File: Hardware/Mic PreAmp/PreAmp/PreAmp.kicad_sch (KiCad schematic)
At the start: 1 part, among them U1 INA217AIDWR

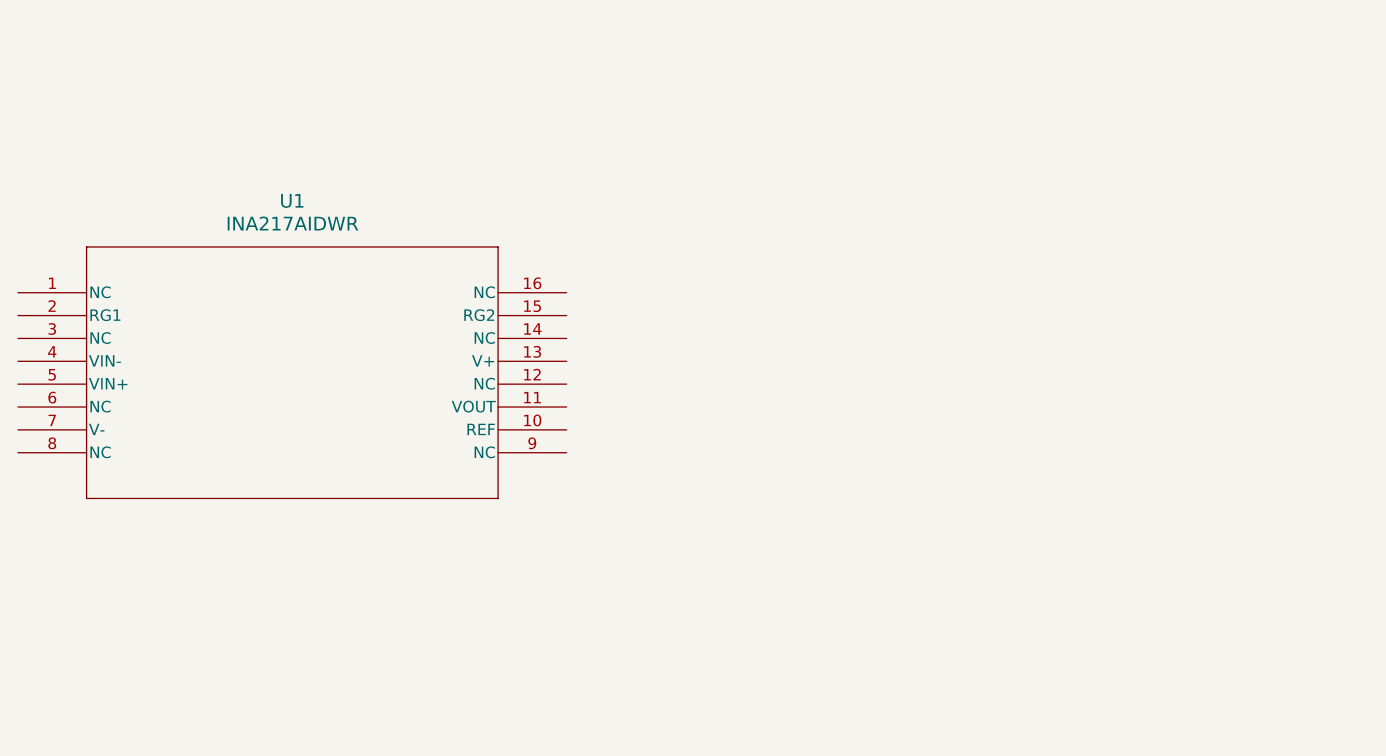
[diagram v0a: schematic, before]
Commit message: Header pins for input and output
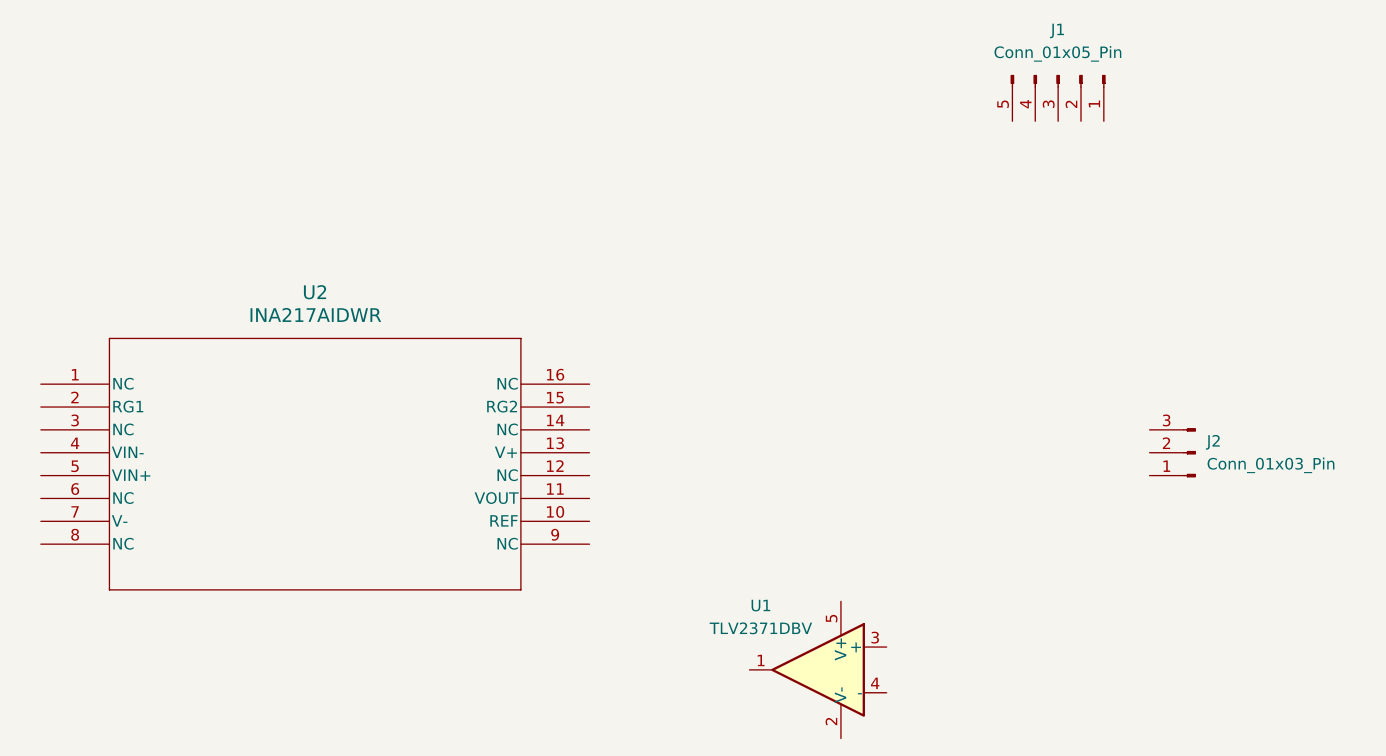
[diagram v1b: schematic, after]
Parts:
- removed U1: INA217AIDWR, DW16, symbol INA217:INA217AIDWR
- added J1: Conn_01x05_Pin, Connector_PinSocket_2.54mm:PinSocket_1x05_P2.54mm_Vertical, symbol Connector:Conn_01x05_Pin
- added J2: Conn_01x03_Pin, symbol Connector:Conn_01x03_Pin
- added U1: TLV2371DBV, Package_TO_SOT_SMD:SOT-23-5, symbol Amplifier_Operational:TLV2371DBV
- added U2: INA217AIDWR, INA217:DW16, symbol INA217:INA217AIDWR
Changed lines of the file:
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@@
 	)
 	(symbol
-		(lib_id "INA217:INA217AIDWR")
-		(at 106.68 81.28 0)
+		(lib_id "Connector:Conn_01x03_Pin")
+		(at 237.49 99.06 180)
 		(unit 1)
 		(exclude_from_sim no)
@@
 		(dnp no)
 		(fields_autoplaced yes)
+		(property "Reference" "J2"
+			(at 238.76 97.7899 0)
+			(effects
+				(font
+					(size 1.27 1.27)
+				)
+				(justify right)
+			)
+		)
+		(property "Value" "Conn_01x03_Pin"
+			(at 238.76 100.3299 0)
+			(effects
+				(font
+					(size 1.27 1.27)
+				)
+				(justify right)
+			)
+		)
+		(property "Footprint" ""
+			(at 237.49 99.06 0)
+			(effects
+				(font
+					(size 1.27 1.27)
+				)
+				(hide yes)
+			)
+		)
+		(property "Datasheet" "~"
+			(at 237.49 99.06 0)
+			(effects
+				(font
+					(size 1.27 1.27)
+				)
+				(hide yes)
+			)
+		)
+		(property "Description" "Generic connector, single row, 01x03, script generated"
+			(at 237.49 99.06 0)
+			(effects
+				(font
+					(size 1.27 1.27)
+				)
+				(hide yes)
+			)
+		)
+		(pin "3"
+		)
+		(pin "2"
+		)
+		(pin "1"
+		)
+		(instances
+			(project ""
+				(path "/c83f892f-6017-40cb-88c0-c4e7a35464f0"
+					(reference "J2")
+					(unit 1)
+				)
+			)
+		)
+	)
+	(symbol
+		(lib_id "INA217:INA217AIDWR")
+		(at 109.22 91.44 0)
+		(unit 1)
+		(exclude_from_sim no)
+		(in_bom yes)
+		(on_board yes)
+		(dnp no)
+		(fields_autoplaced yes)
+		(property "Reference" "U2"
+			(at 139.7 81.28 0)
+			(effects
+				(font
+					(size 1.524 1.524)
+				)
+			)
+		)
+		(property "Value" "INA217AIDWR"
+			(at 139.7 83.82 0)
+			(effects
+				(font
+					(size 1.524 1.524)
+				)
+			)
+		)
+		(property "Footprint" "INA217:DW16"
+			(at 109.22 91.44 0)
+			(effects
+				(font
+					(size 1.27 1.27)
+					(italic yes)
+				)
+				(hide yes)
+			)
+		)
+		(property "Datasheet" "INA217AIDWR"
+			(at 109.22 91.44 0)
+			(effects
+				(font
+					(size 1.27 1.27)
+					(italic yes)
+				)
+				(hide yes)
+			)
+		)
+		(property "Description" ""
+			(at 109.22 91.44 0)
+			(effects
+				(font
+					(size 1.27 1.27)
+				)
+				(hide yes)
+			)
+		)
+		(pin "13"
+		)
+		(pin "11"
+		)
+		(pin "12"
+		)
+		(pin "3"
+		)
+		(pin "4"
+		)
+		(pin "5"
+		)
+		(pin "6"
+		)
+		(pin "7"
+		)
+		(pin "8"
+		)
+		(pin "1"
+		)
+		(pin "9"
+		)
+		(pin "14"
+		)
+		(pin "15"
+		)
+		(pin "2"
+		)
+		(pin "10"
+		)
+		(pin "16"
+		)
+		(instances
+			(project ""
+				(path "/c83f892f-6017-40cb-88c0-c4e7a35464f0"
+					(reference "U2")
+					(unit 1)
+				)
+			)
+		)
+	)
+	(symbol
+		(lib_id "Amplifier_Operational:TLV2371DBV")
+		(at 195.58 123.19 0)
+		(mirror y)
+		(unit 1)
+		(exclude_from_sim no)
+		(in_bom yes)
+		(on_board yes)
+		(dnp no)
 		(property "Reference" "U1"
-			(at 137.16 71.12 0)
-			(effects
-				(font
-					(size 1.524 1.524)
-				)
-			)
-		)
-		(property "Value" "INA217AIDWR"
-			(at 137.16 73.66 0)
-			(effects
-				(font
-					(size 1.524 1.524)
-				)
-			)
-		)
-		(property "Footprint" "DW16"
-			(at 106.68 81.28 0)
-			(effects
-				(font
-					(size 1.27 1.27)
-					(italic yes)
-				)
-				(hide yes)
-			)
-		)
-		(property "Datasheet" "INA217AIDWR"
-			(at 106.68 81.28 0)
-			(effects
-				(font
-					(size 1.27 1.27)
-					(italic yes)
-				)
-				(hide yes)
-			)
-		)
-		(property "Description" ""
-			(at 106.68 81.28 0)
+			(at 189.23 116.078 0)
+			(effects
+				(font
+					(size 1.27 1.27)
+				)
+			)
+		)
+		(property "Value" "TLV2371DBV"
+			(at 189.23 118.618 0)
+			(effects
+				(font
+					(size 1.27 1.27)
+				)
+			)
+		)
+		(property "Footprint" "Package_TO_SOT_SMD:SOT-23-5"
+			(at 198.12 128.27 0)
+			(effects
+				(font
+					(size 1.27 1.27)
+				)
+				(justify left)
+				(hide yes)
+			)
+		)
+		(property "Datasheet" "http://www.ti.com/lit/ds/symlink/tlv2375.pdf"
+			(at 195.58 118.11 0)
+			(effects
+				(font
+					(size 1.27 1.27)
+				)
+				(hide yes)
+			)
+		)
+		(property "Description" "Rail-to-Rail Input/Output Operational Amplifier, SOT-23-5"
+			(at 195.58 123.19 0)
 			(effects
 				(font
@@
 		(pin "3"
 		)
-		(pin "10"
-		)
-		(pin "15"
-		)
-		(pin "12"
-		)
-		(pin "11"
-		)
-		(pin "6"
-		)
-		(pin "7"
-		)
-		(pin "8"
-		)
-		(pin "16"
-		)
-		(pin "9"
+		(pin "5"
+		)
+		(pin "1"
+		)
+		(pin "4"
 		)
 		(pin "2"
-		)
-		(pin "4"
-		)
-		(pin "13"
-		)
-		(pin "5"
-		)
-		(pin "1"
-		)
-		(pin "14"
 		)
 		(instances
@@
 					(unit 1)
 				)
+			)
+		)
+	)
+	(symbol
+		(lib_id "Connector:Conn_01x05_Pin")
+		(at 222.25 57.15 270)
+		(unit 1)
+		(exclude_from_sim no)
+		(in_bom yes)
+		(on_board yes)
+		(dnp no)
+		(fields_autoplaced yes)
+		(property "Reference" "J1"
+			(at 222.25 52.07 90)
+			(effects
+				(font
+					(size 1.27 1.27)
+				)
+			)
+		)
+		(property "Value" "Conn_01x05_Pin"
+			(at 222.25 54.61 90)
+			(effects
+				(font
+					(size 1.27 1.27)
+				)
+			)
+		)
+		(property "Footprint" "Connector_PinSocket_2.54mm:PinSocket_1x05_P2.54mm_Vertical"
+			(at 222.25 57.15 0)
+			(effects
+				(font
+					(size 1.27 1.27)
+				)
+				(hide yes)
+			)
+		)
+		(property "Datasheet" "~"
+			(at 222.25 57.15 0)
+			(effects
+				(font
+					(size 1.27 1.27)
+				)
+				(hide yes)
+			)
+		)
+		(property "Description" "Generic connector, single row, 01x05, script generated"
+			(at 222.25 57.15 0)
+			(effects
+				(font
+					(size 1.27 1.27)
+				)
+				(hide yes)
+			)
+		)
+		(pin "2"
+		)
+		(pin "1"
+		)
+		(pin "5"
+		)
+		(pin "4"
+		)
+		(pin "3"
+		)
+		(instances
+			(project ""
+				(path "/c83f892f-6017-40cb-88c0-c4e7a35464f0"
+					(reference "J1")
+					(unit 1)
+				)

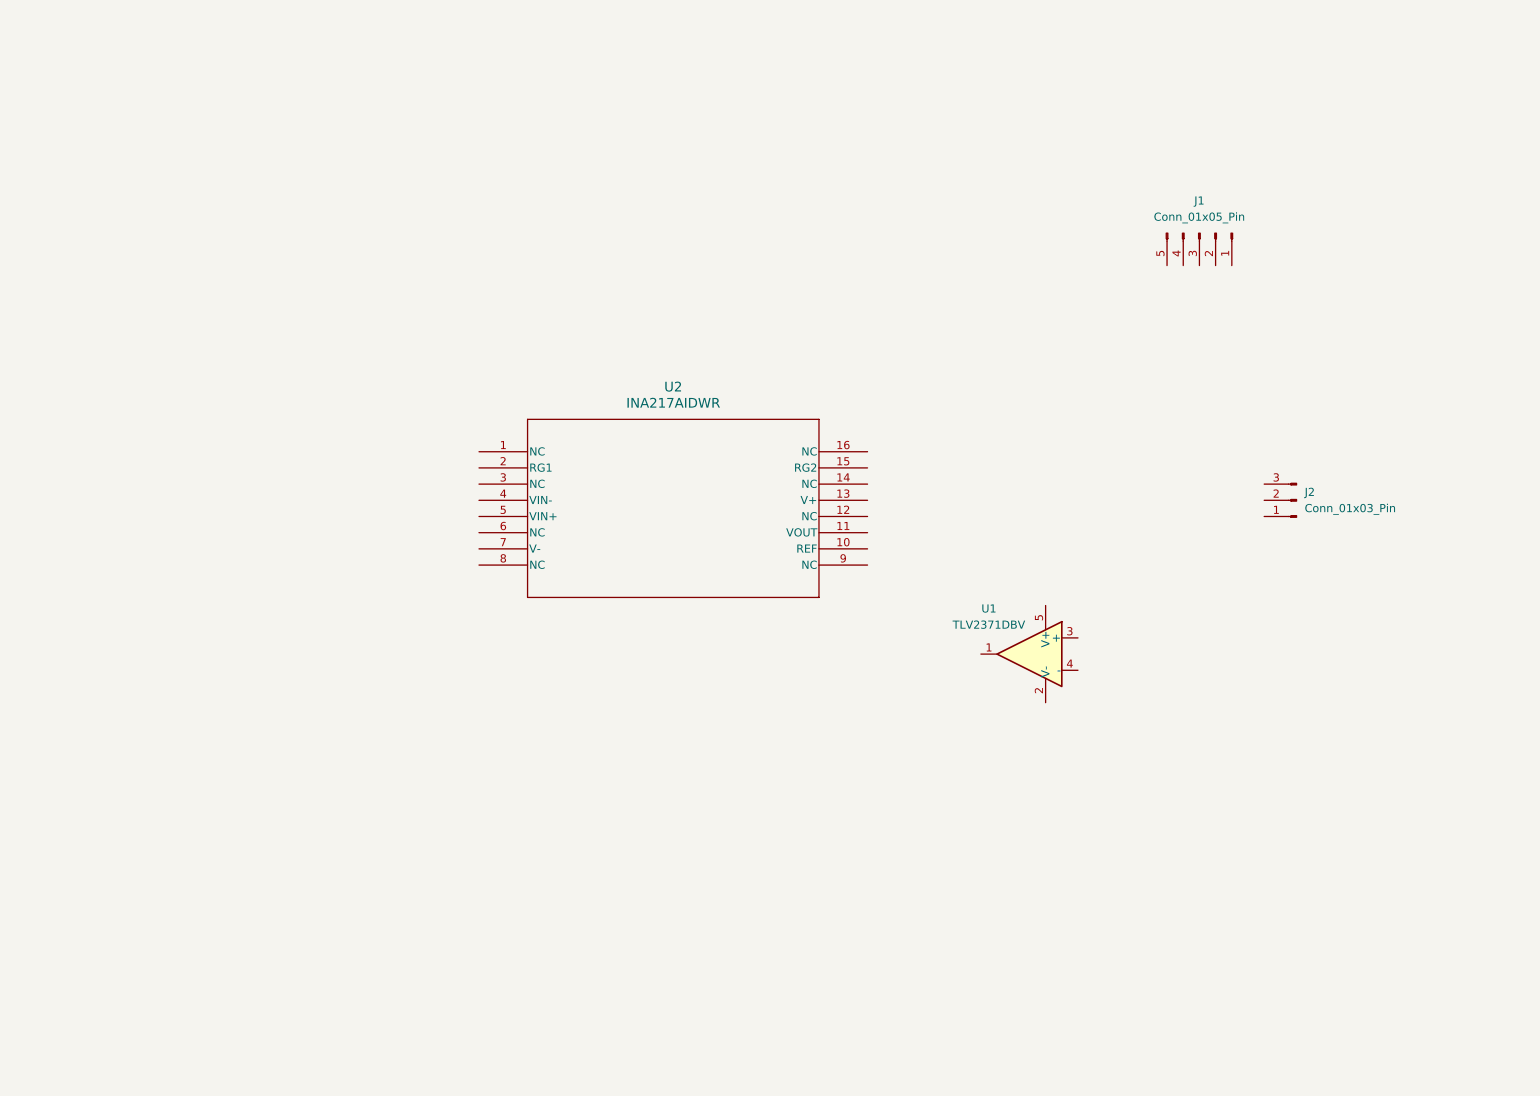
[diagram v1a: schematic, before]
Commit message: Inserted XLR plug
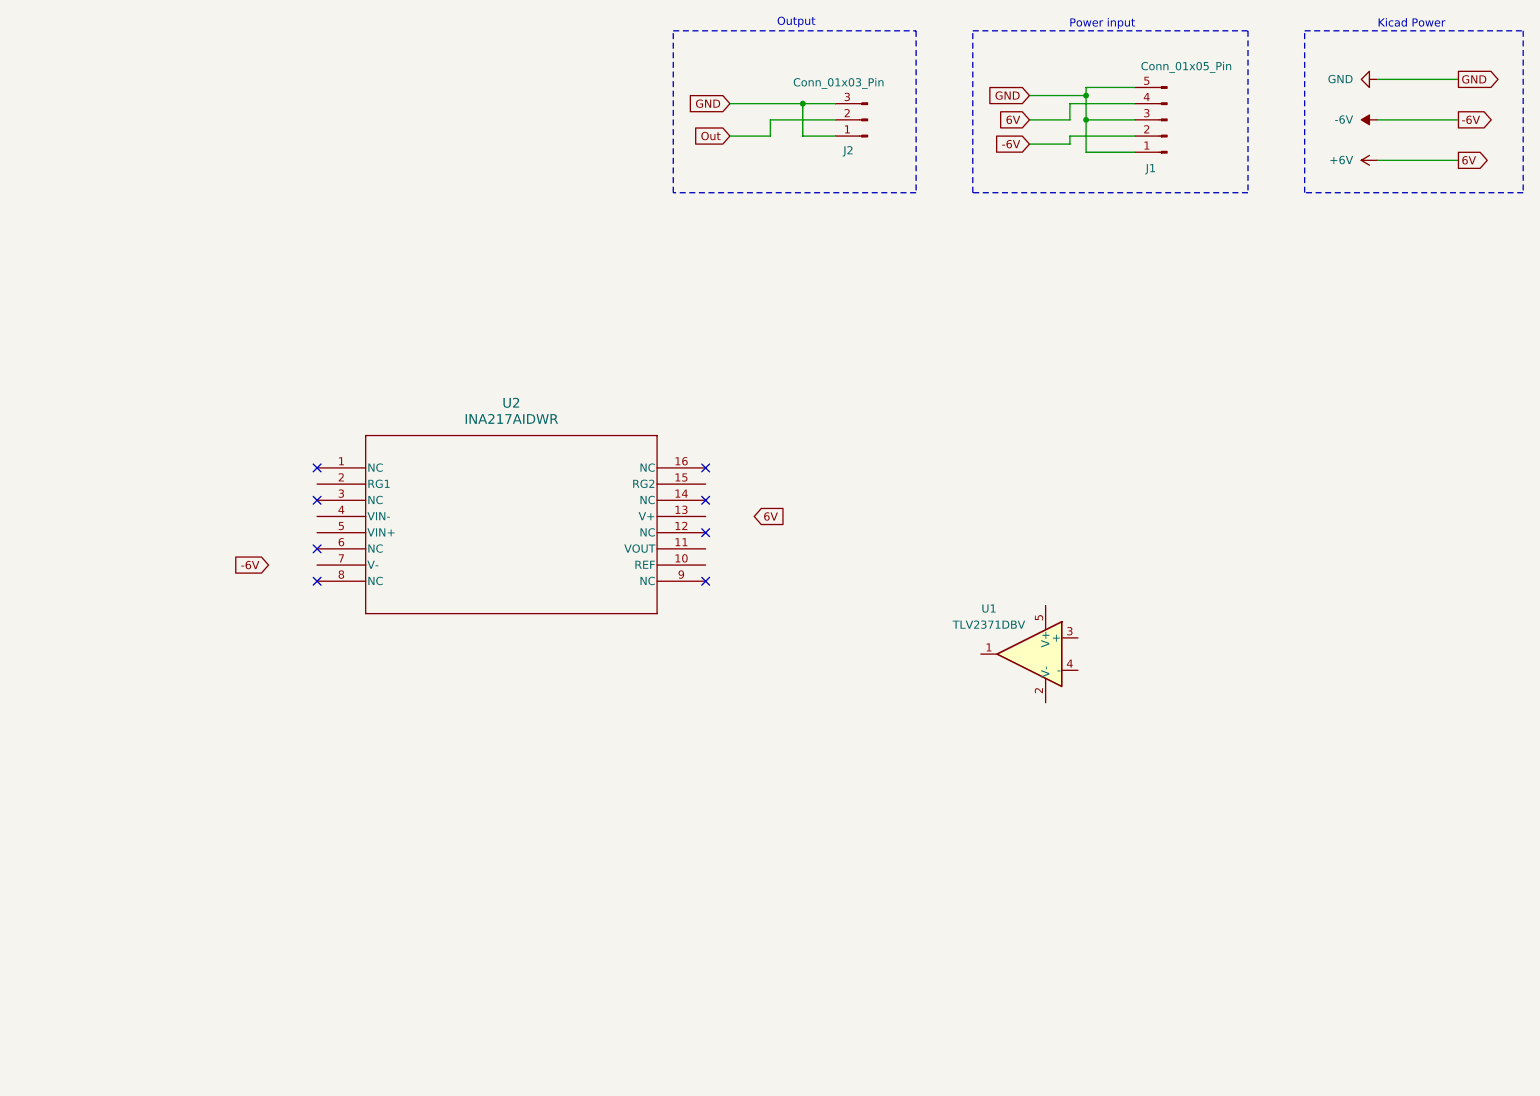
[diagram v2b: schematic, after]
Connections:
- net GND: now reaches J2.1 (Pin_1)
- net GND: now also J1.1 (Pin_1), J1.3 (Pin_3), J1.5 (Pin_5), J2.3 (Pin_3)
- net Out: now reaches J2.2 (Pin_2)
- net -6V: now reaches J1.2 (Pin_2)
- net +6V: now reaches J1.4 (Pin_4)
- no-connect marks 0 -> 8
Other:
- note added: "Kicad Power"
- note added: "Output"
- note added: "Power input"
- moved on the sheet: J1, J2, U2

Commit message: created XLR input
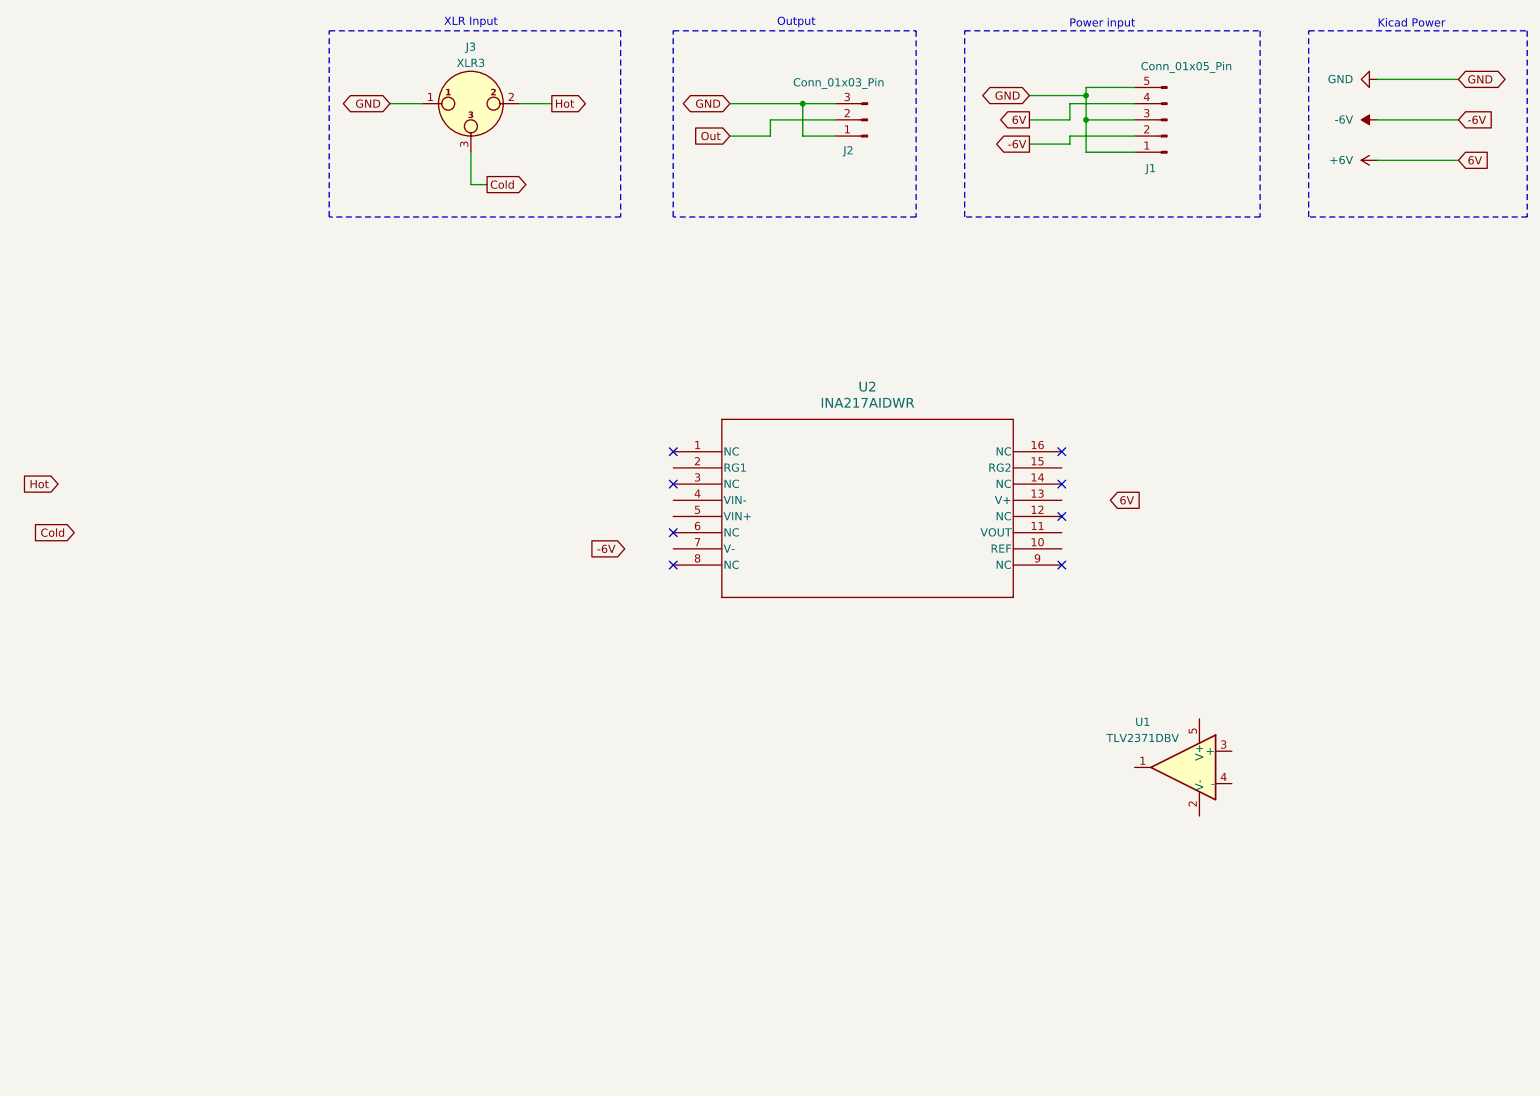
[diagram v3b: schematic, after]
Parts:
- added J3: XLR3, Connector_Audio:Jack_XLR_Neutrik_NC3FAAV-0_Vertical, symbol Connector_Audio:XLR3
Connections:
- net GND: now also J3.1
- new net Cold: J3.3
- new net Hot: J3.2
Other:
- note added: "XLR Input"
- moved on the sheet: U1, U2
